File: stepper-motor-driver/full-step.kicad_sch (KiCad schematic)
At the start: 8 parts, among them U1 74HC14, U2 74LS163, U3 74LS00, U4 74LS86, U5 74HC14, U6 74HC14, U7 74HC14, U8 LM7805_TO220

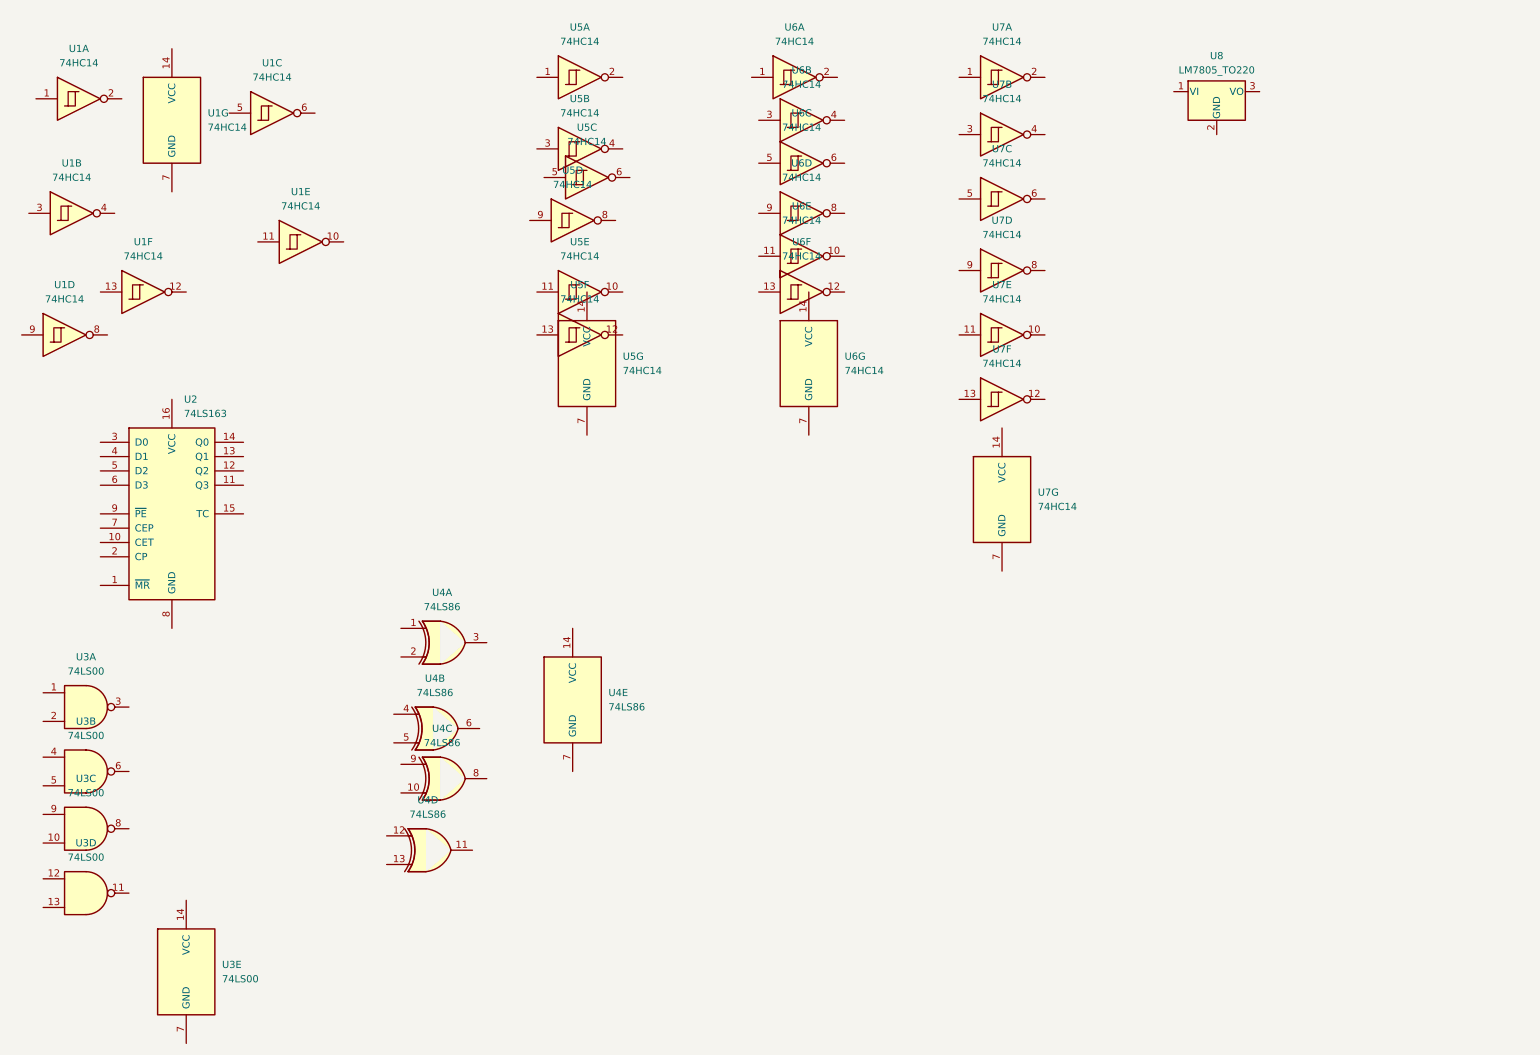
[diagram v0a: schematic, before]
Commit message: schematic mostly done except gate drivers
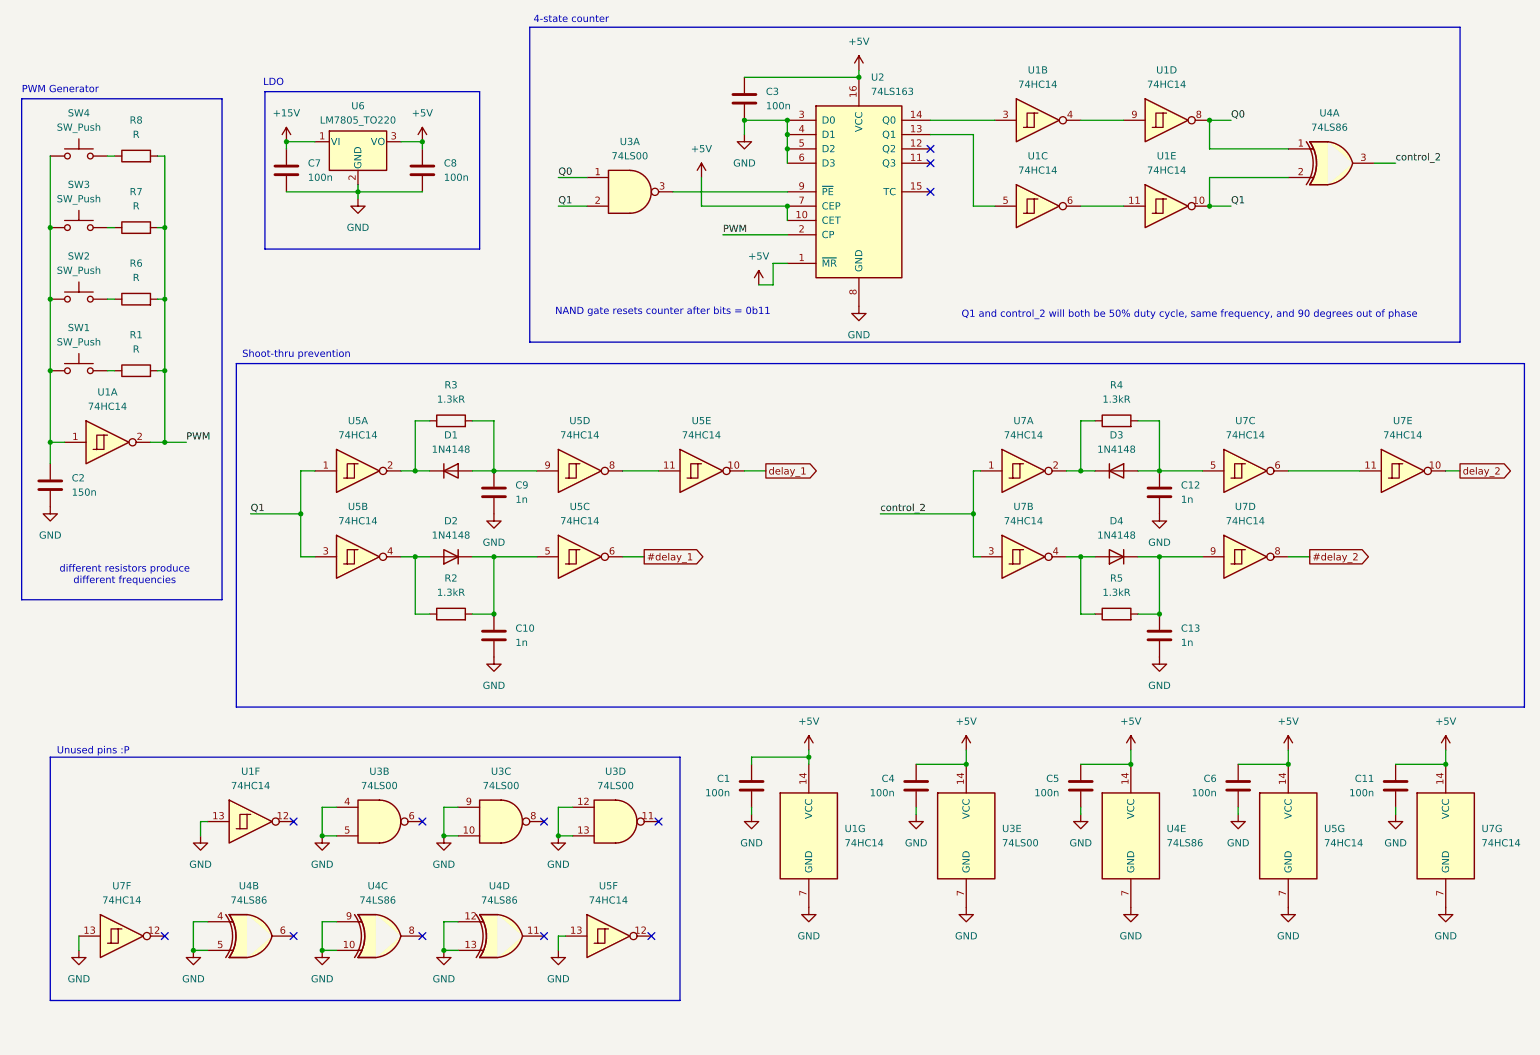
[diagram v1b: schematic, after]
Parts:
- removed U6: 74HC14, symbol 74xx:74HC14
- removed U8: LM7805_TO220, Package_TO_SOT_THT:TO-220-3_Vertical, symbol Regulator_Linear:LM7805_TO220
- added C1, C11, C3, C4, C5, C6, C7, C8: 100n, symbol Device:C
- added C10, C12, C13, C9: 1n, symbol Device:C
- added C2: 150n, symbol Device:C
- added D1, D2, D3, D4: 1N4148, Diode_THT:D_DO-35_SOD27_P7.62mm_Horizontal, symbol Diode:1N4148
- added R1, R6, R7, R8: R, symbol Device:R
- added R2, R3, R4, R5: 1.3kR, symbol Device:R
- added SW1, SW2, SW3, SW4: SW_Push, symbol Switch:SW_Push
- added U6: LM7805_TO220, Package_TO_SOT_THT:TO-220-3_Vertical, symbol Regulator_Linear:LM7805_TO220
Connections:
- net GND: now reaches U5.13
- net GND: now also U1.13, U1.7 (GND), U2.3 (D0), U2.4 (D1), U2.5 (D2), U2.6 (D3), U2.8 (GND), U3.10, U3.12, U3.13, U3.4, U3.5, U3.7 (GND), U3.9, U4.10, U4.12, U4.13, U4.4, U4.5, U4.7 (GND), U4.9, U5.7 (GND), U7.13, U7.7 (GND), C1.2, C10.2, C11.2, C12.2, C13.2, C2.2, C3.2, C4.2, C5.2, C6.2, C7.2, C8.2, C9.2, U6.2 (GND)
- net +5V: now reaches U3.14 (VCC)
- net +5V: now also U1.14 (VCC), U2.1 (~{MR}), U2.10 (CET), U2.16 (VCC), U2.7 (CEP), U4.14 (VCC), U5.14 (VCC), U7.14 (VCC), C1.1, C11.1, C3.1, C4.1, C5.1, C6.1, C8.1, U6.3 (VO)
- net Q1: now reaches U5.3
- net Q1: now also U1.10, U3.2, U4.2, U5.1
- net at U5.4: now also D2.2 (A), R2.1
- net control_2: now reaches U7.1
- net control_2: now also U4.3, U7.3
- net at U7.2: now also D3.1 (K), R4.1
- net #delay_2: now reaches U7.8
- net at U7.9: now also C13.1, D4.1 (K), R5.2
- net at U5.2: now also D1.1 (K), R3.1
- net at U5.5: now also C10.1, D2.1 (K), R2.2
- net #delay_1: now reaches U5.6
- net delay_2: now reaches U7.10
- net at U7.11: now also U7.6
- net Q0: now reaches U4.1
- net Q0: now also U1.8, U3.1
- net at U3.3: now also U2.9 (~{PE})
- net at U5.8: now also U5.11
- net at U5.9: now also C9.1, D1.2 (A), R3.2
- net at U7.5: now also C12.1, D3.2 (A), R4.2
- net at U1.9: now also U1.4
- net at U1.11: now also U1.6
- net at U1.5: now also U2.13 (Q1)
- net at U7.4: now also D4.2 (A), R5.1
- net delay_1: now reaches U5.10
- net at U1.1: now also C2.1, SW1.1, SW2.1, SW3.1, SW4.1
- net PWM: now reaches U1.2
- net PWM: now also U2.2 (CP), R1.2, R6.2, R7.2, R8.2
- net at U1.3: now also U2.14 (Q0)
- new net: R6.1, SW2.2
- new net: R7.1, SW3.2
- new net: R1.1, SW1.2
- new net: R8.1, SW4.2
- new net +15V: C7.1, U6.1 (VI)
- no-connect marks 0 -> 12
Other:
- note added: "4-state counter"
- note added: "LDO"
- note added: "NAND gate resets counter after bits = 0b11"
- note added: "PWM Generator"
- note added: "Q1 and control_2 will both be 50% duty cycle, same frequency, and 90 degrees out of phase"
- note added: "Shoot-thru prevention"
- note added: "Unused pins :P"
- note added: "different resistors produce different frequencies"
